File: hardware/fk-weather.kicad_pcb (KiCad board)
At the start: 2 copper layers, 26.2 x 121.2 mm, 65 parts, among them J1 RJ11-6, J2 MICRO-USB, J3 RJ11-6, J4 CONN-HDR-1x19, J5 CONN-HDR-1x19, J6 CONN-HDR-2x5, M1 MOUNT_HOLE, M2 MOUNT_HOLE, M3 MOUNT_HOLE, M4 MOUNT_HOLE, P1 CONN-HDR-MODULE, Q1 2N7002LT1G, SW1 SPNO, U1 ATSAMD21G18A-AU, U2 BQ24074RGTT, U4 MCP1700T-3302E/MB, Y1 FC-135

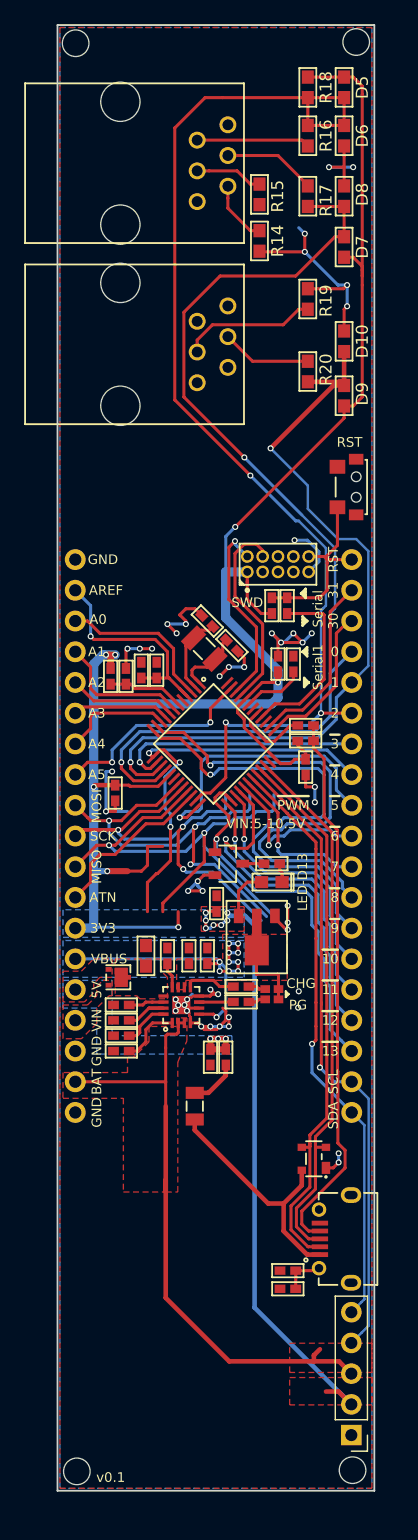
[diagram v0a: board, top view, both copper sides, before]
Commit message: Starting on the basic sensor module board. Just IC stuff.
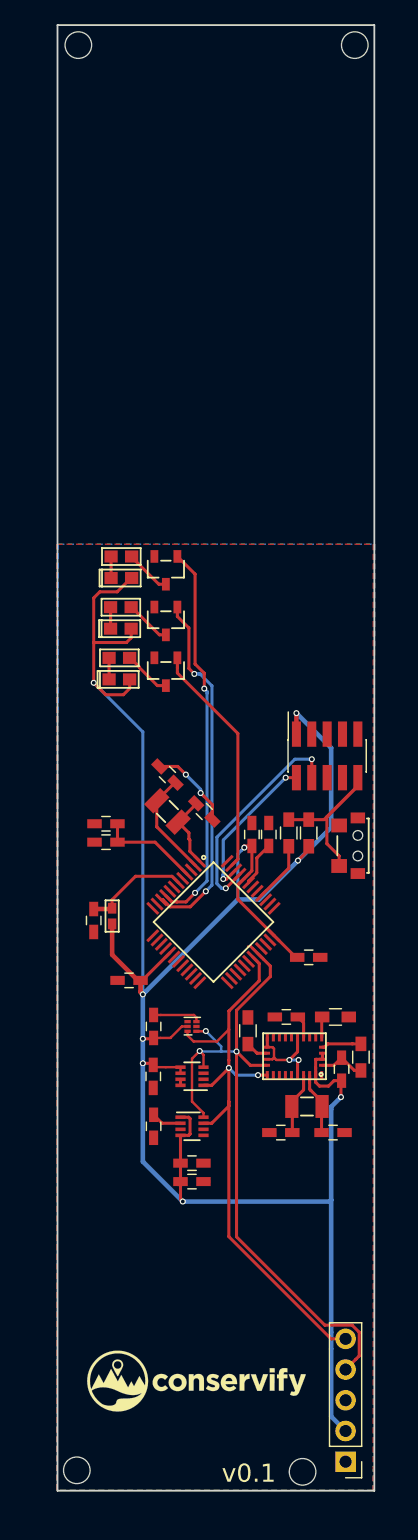
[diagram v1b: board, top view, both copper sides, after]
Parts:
- removed C10, C17: 4.7uF 10V X5R, RocketScreamKicadLibrary:CAP-0402
- removed C15, C19: 1uF 10V X5R, RocketScreamKicadLibrary:CAP-0402
- removed C18: 4.7nF 25V X7R, RocketScreamKicadLibrary:CAP-0402
- removed C9: 1uF 50V X5R, RocketScreamKicadLibrary:CAP-0603
- removed D10, D5, D6, D7, D8, D9: BAS16, RocketScreamKicadLibrary:DIO-0603
- removed D4: PMEG3020CPA, RocketScreamKicadLibrary:SOT-1016
- removed F1: MF-PSMF050X-2, RocketScreamKicadLibrary:MF-PSMF020X
- removed J1, J3: RJ11-6, fk-weather:molex_95501-2641
- removed J2: MICRO-USB, RocketScreamKicadLibrary:MICRO-USB
- removed J4, J5: CONN-HDR-1x19, RocketScreamKicadLibrary:HDR_1x19_Pitch2.54mm_WithoutSilk
- removed L1: BKP1005TS121-T, RocketScreamKicadLibrary:IND-0402
- removed P1: CONN-HDR-MODULE, fk-core-mini-ultra-pro:Socket_Strip_Straight_1x05_Pitch2.54mm
- removed R10, R13: 2K2, RocketScreamKicadLibrary:RES-0402
- removed R11: 100K, RocketScreamKicadLibrary:RES-0402
- removed R12, R8: 10K, RocketScreamKicadLibrary:RES-0402
- removed R14, R15, R16, R17, R19, R20: 1K, RocketScreamKicadLibrary:RES-0603
- removed R18: 4.7K, RocketScreamKicadLibrary:RES-0603
- removed R6: 1K18, RocketScreamKicadLibrary:RES-0402
- removed R7: 46K4, RocketScreamKicadLibrary:RES-0402
- removed R9: 2K94, RocketScreamKicadLibrary:RES-0402
- removed U2: BQ24074RGTT, RocketScreamKicadLibrary:QFN-16_3x3mm
- removed U4: MCP1700T-3302E/MB, RocketScreamKicadLibrary:SOT-89
- added C101: 1uF, Capacitors_SMD:C_0603_HandSoldering, F.Cu at (134.7, 114.8)
- added C102: 100nF, Capacitors_SMD:C_0603_HandSoldering, F.Cu at (134.7, 123.1)
- added C103: 100nF, Capacitors_SMD:C_0603_HandSoldering, F.Cu at (137.9, 127.6)
- added C104: 10uF, Capacitors_SMD:C_0603_HandSoldering, F.Cu at (137.9, 126.1)
- added C105: 22pF, Capacitors_SMD:C_0603_HandSoldering, F.Cu at (149.6, 123.6)
- added C106: 100nF, Capacitors_SMD:C_0603_HandSoldering, F.Cu at (150.3, 118.3)
- added C107: 22pF, Capacitors_SMD:C_0603_HandSoldering, F.Cu at (145.3, 123.6)
- added C108: 100nF, Capacitors_SMD:C_0603_HandSoldering, F.Cu at (145.7, 114.0)
- added C109: 100nF, Capacitors_SMD:C_0603_HandSoldering, F.Cu at (134.7, 118.9)
- added G***: LOGO, conservify:conservify_text_negative_4000, F.Cu at (138.3, 144.1)
- added P101: CONN_01X05, Socket_Strips:Socket_Strip_Straight_1x05_Pitch2.54mm, F.Cu at (150.6, 150.8)
- added Q2: 2N7002LT1G, RocketScreamKicadLibrary:SOT-23, F.Cu at (135.8, 81.3)
- added Q3: 2N7002LT1G, RocketScreamKicadLibrary:SOT-23, F.Cu at (135.8, 85.5)
- added R101: 10K, Resistors_SMD:R_0603_HandSoldering, F.Cu at (142.5, 115.2)
- added R102: 10K, Resistors_SMD:R_0603_HandSoldering, F.Cu at (149.8, 114.0)
- added R103: 10K, Resistors_SMD:R_0603_HandSoldering, F.Cu at (151.9, 117.3)
- added U101: TSL2591, Housings_DFN_QFN:DFN-6-1.3x1.2mm_Pitch0.4mm, F.Cu at (137.9, 114.8)
- added U102: MPL3115A2, Housings_DFN_QFN:DFN-8_2x2mm_Pitch0.5mm, F.Cu at (137.9, 123.1)
- added U103: BNO055, conservify:BNO055, F.Cu at (146.4, 117.3)
- added U104: SHT31, Housings_DFN_QFN:DFN-8_2x2mm_Pitch0.5mm, F.Cu at (137.9, 118.9)
- added Y101: FC-135, RocketScreamKicadLibrary:ABS07, F.Cu at (147.4, 121.4)
- C1, C14, C2, C3, C4, C5, C6, C7, C8: footprint RocketScreamKicadLibrary:CAP-0402 -> Capacitors_SMD:C_0603_HandSoldering
- D2: value LED-DUAL -> Yellow; footprint RocketScreamKicadLibrary:LED-1615 -> RocketScreamKicadLibrary:LED-0603
- D3: value PRTR5V0U2X -> Blue; footprint RocketScreamKicadLibrary:SOT-143B -> RocketScreamKicadLibrary:LED-0603
- J6: footprint RocketScreamKicadLibrary:HDR_2x5_Pitch1.27mm -> Socket_Strips:Socket_Strip_Straight_2x05_Pitch1.27mm_SMD
- R1: value 2K2 -> 2k2; footprint RocketScreamKicadLibrary:RES-0402 -> RocketScreamKicadLibrary:RES-0603
- R2, R4: footprint RocketScreamKicadLibrary:RES-0402 -> Resistors_SMD:R_0603_HandSoldering
- R3: value 330R -> 2k2; footprint RocketScreamKicadLibrary:RES-0402 -> RocketScreamKicadLibrary:RES-0603
- R5: value 1M -> 2k2; footprint RocketScreamKicadLibrary:RES-0402 -> RocketScreamKicadLibrary:RES-0603
- moved M4 120.3 mm to (128.4, 151.5)
- moved M2 117.8 mm to (151.4, 33.7)
- moved R5 54.0 mm to (131.9, 84.3), turned to 0 degrees
- moved D3 42.8 mm to (131.9, 86.1), turned to 0 degrees
- moved D2 32.7 mm to (132.0, 81.9), turned to 0 degrees
- moved SW1 29.7 mm to (151.8, 99.9)
- moved R1 28.3 mm to (132.1, 75.9), turned to 0 degrees
- moved D1 28.1 mm to (132.1, 77.7), turned to 0 degrees
- moved Q1 24.8 mm to (135.8, 77.1), turned to 180 degrees
- moved C4 20.4 mm to (129.8, 106.0), turned to 270 degrees
- moved L2 19.8 mm to (131.3, 105.7), turned to 270 degrees
- moved R4 19.0 mm to (147.6, 98.8)
- moved R2 18.8 mm to (145.9, 98.8)
- moved M1 18.7 mm to (147.1, 151.6)
- moved R3 18.1 mm to (132.0, 80.1), turned to 0 degrees
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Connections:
- D2 pad 1: VBUS -> Net-(D2-Pad1)
- D2 pad 2: VBUS -> 3V3
- D3 pad 1: GND -> Net-(D3-Pad1)
- D3 pad 2: /USB+ -> 3V3
- J6 pad 6: (no net) -> Net-(J6-Pad6)
- J6 pad 7: (no net) -> Net-(J6-Pad7)
- J6 pad 8: (no net) -> Net-(J6-Pad8)
- Q1 pad 1: /D13 -> /A3
- R3 pad 1: Net-(J2-Pad4) -> Net-(D2-Pad1)
- R3 pad 2: /USB_ID -> Net-(Q2-Pad3)
- R5 pad 1: Net-(C18-Pad1) -> Net-(D3-Pad1)
- R5 pad 2: GND -> Net-(Q3-Pad3)
- U1 pad 26: /D13 -> Net-(U1-Pad26)
- U1 pad 39: (no net) -> /TX_LED
- U1 pad 48: (no net) -> /RX_LED
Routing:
- net /D2: track 95.3 -> 0.00 mm, vias 3 -> 0
- net /D0: track 87.0 -> 0.00 mm, vias 2 -> 0
- net /D1: track 64.8 -> 0.00 mm, vias 2 -> 0
- net GND: track 86.0 -> 24.6 mm, vias 46 -> 4
- net VBAT: track 51.7 -> 0.00 mm
- net Net-(J2-Pad4): track 45.5 -> 0.00 mm
- net /USB-: track 45.4 -> 0.00 mm
- net /MISO: track 45.3 -> 0.00 mm, vias 2 -> 0
- net /USB+: track 44.8 -> 0.00 mm
- net /D9: track 40.2 -> 0.00 mm, vias 1 -> 0
- net /SCK: track 37.4 -> 0.00 mm, vias 3 -> 0
- net /MOSI: track 37.2 -> 0.00 mm, vias 3 -> 0
- net /D8: track 37.0 -> 0.00 mm, vias 1 -> 0
- net VBUS: track 35.4 -> 0.00 mm, vias 11 -> 0
- net /D4: track 35.0 -> 0.00 mm, vias 3 -> 0
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- removed copper zone on B.Cu, net 3V3
- removed copper zone on F.Cu, net 3V3
- removed copper zone on B.Cu, net 5V0
- removed copper zone on F.Cu, net 5V0
- removed copper zone on F.Cu, net VBAT
- removed copper zone on B.Cu, net VBUS
- removed copper zone on F.Cu, net VBUS
- removed copper zone on F.Cu, net VEXT
- removed copper zone on F.Cu, net VIN
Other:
- board text removed: "0"
- board text removed: "1"
- board text removed: "10"
- board text removed: "11"
- board text removed: "12"
- board text removed: "13"
- board text removed: "2"
- board text removed: "3"
- board text removed: "30"
- board text removed: "31"
- board text removed: "3V3"
- board text removed: "4"
- board text removed: "5"
- board text removed: "5V"
- board text removed: "6"
- board text removed: "7"
- board text removed: "8"
- board text removed: "9"
- board text removed: "A0"
- board text removed: "A1"
- board text removed: "A2"
- board text removed: "A3"
- board text removed: "A4"
- board text removed: "A5"
- board text removed: "AREF"
- board text removed: "ATN"
- board text removed: "BAT"
- board text removed: "CHG"
- board text removed: "GND"
- board text removed: "LED-D13"
- board text removed: "MISO"
- board text removed: "MOSI"
- board text removed: "PG"
- board text removed: "PWM"
- board text removed: "RST"
- board text removed: "SCK"
- board text removed: "SCL"
- board text removed: "SDA"
- board text removed: "SWD"
- board text removed: "Serial"
- board text removed: "Serial1"
- board text removed: "VBUS"
- board text removed: "VIN"
- board text removed: "VIN:5-10.5V"

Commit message: Adding pull ups, fixing the outline. Plotting.
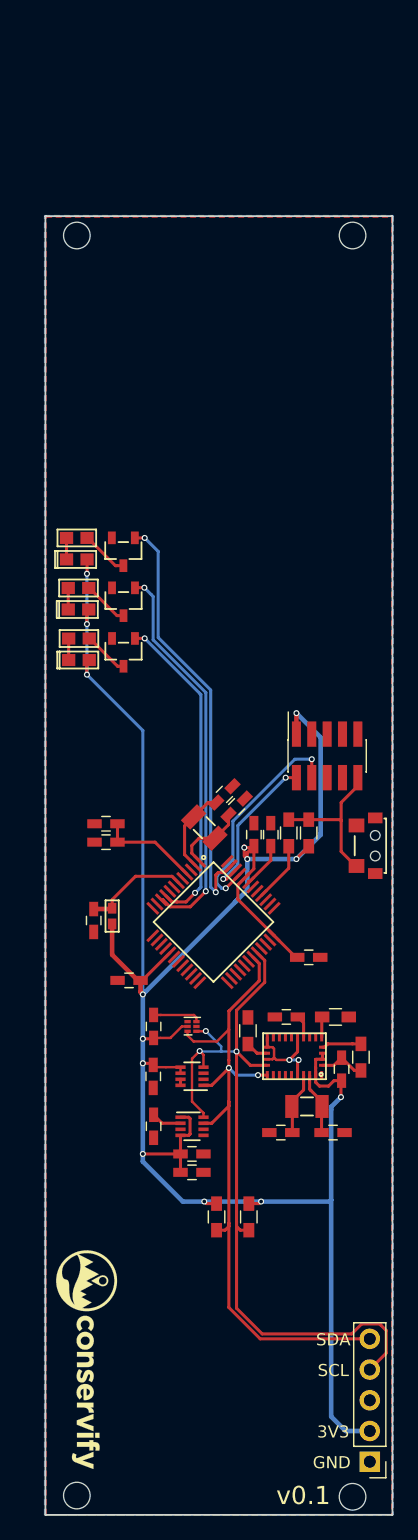
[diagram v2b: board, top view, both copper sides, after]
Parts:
- added R6: 4.7k, Resistors_SMD:R_0603_HandSoldering, F.Cu at (140.0, 130.6)
- added R7: 4.7k, Resistors_SMD:R_0603_HandSoldering, F.Cu at (142.6, 130.6)
- moved M2 120.0 mm to (151.2, 153.7)
- moved M4 104.6 mm to (151.2, 49.4)
- moved M1 18.8 mm to (128.4, 153.6)
- moved M3 15.7 mm to (128.4, 49.4)
- moved D3 10.5 mm to (128.4, 76.2)
- moved Q3 10.5 mm to (132.2, 75.6)
- moved R5 10.5 mm to (128.4, 74.4)
- moved G*** 9.28 mm to (129.2, 142.4), turned to 270 degrees
- moved Q1 7.63 mm to (132.3, 83.9)
- moved R1 7.63 mm to (128.6, 82.7)
- moved D1 7.63 mm to (128.6, 84.5)
- moved C1 4.99 mm to (140.6, 95.6), turned to 225 degrees
- moved D2 3.85 mm to (128.5, 80.3)
- moved R3 3.85 mm to (128.5, 78.5)
- moved Q2 3.85 mm to (132.3, 79.7)
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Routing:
- net /A5: track 19.5 -> 35.6 mm, vias 0 -> 2
- net GND: track 24.6 -> 17.1 mm, vias 4 -> 2
- net /SDA: track 51.1 -> 57.9 mm
- net /SCL: track 59.6 -> 66.4 mm
- net /A3: track 32.2 -> 26.9 mm
- net /A4: track 29.6 -> 32.4 mm
- net /RST: track 15.7 -> 13.0 mm
- net 3V3: track 193.0 -> 190.6 mm, vias 9 -> 14
- net Net-(C1-Pad2): track 8.86 -> 7.08 mm
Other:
- board size 26.2 x 121.2 mm -> 28.7 x 107.4 mm
- board text added: "3V3"
- board text added: "GND"
- board text added: "SCL"
- board text added: "SDA"

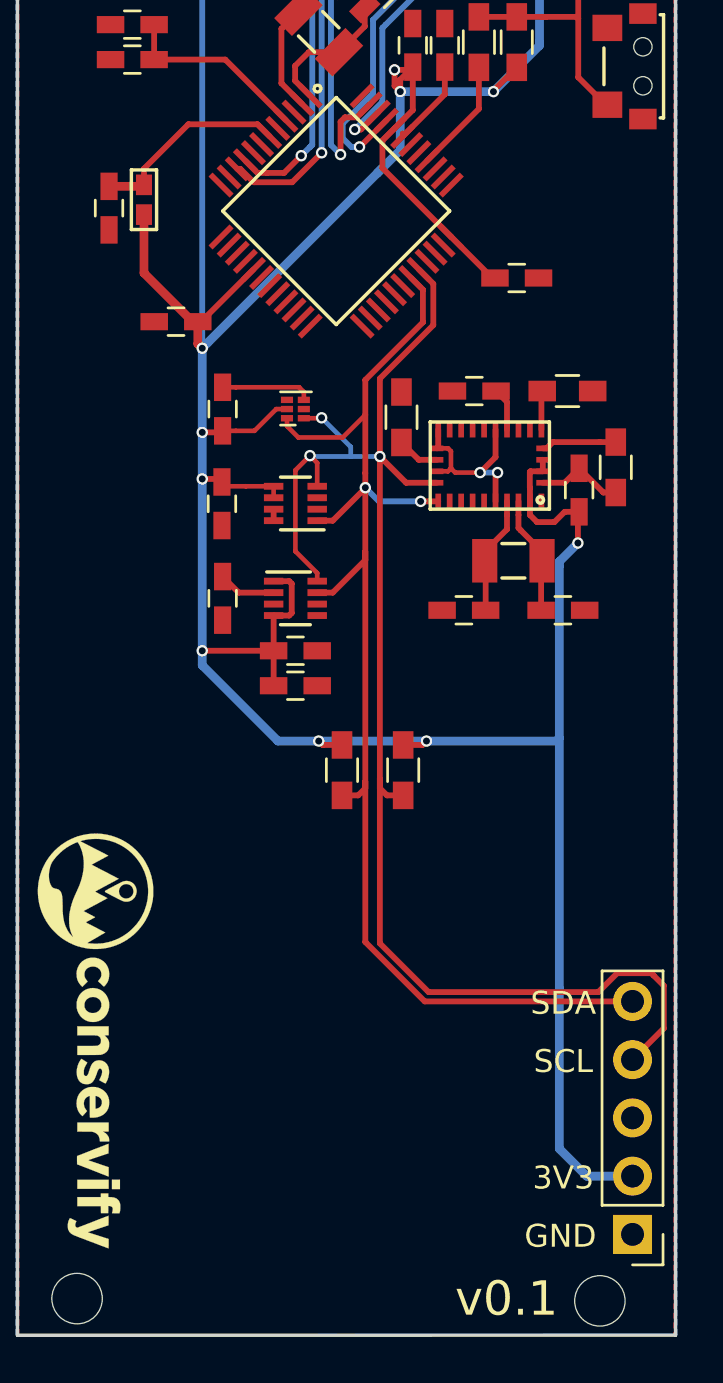
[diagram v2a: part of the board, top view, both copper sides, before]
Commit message: Adding USB connector and 3v3 regulator.
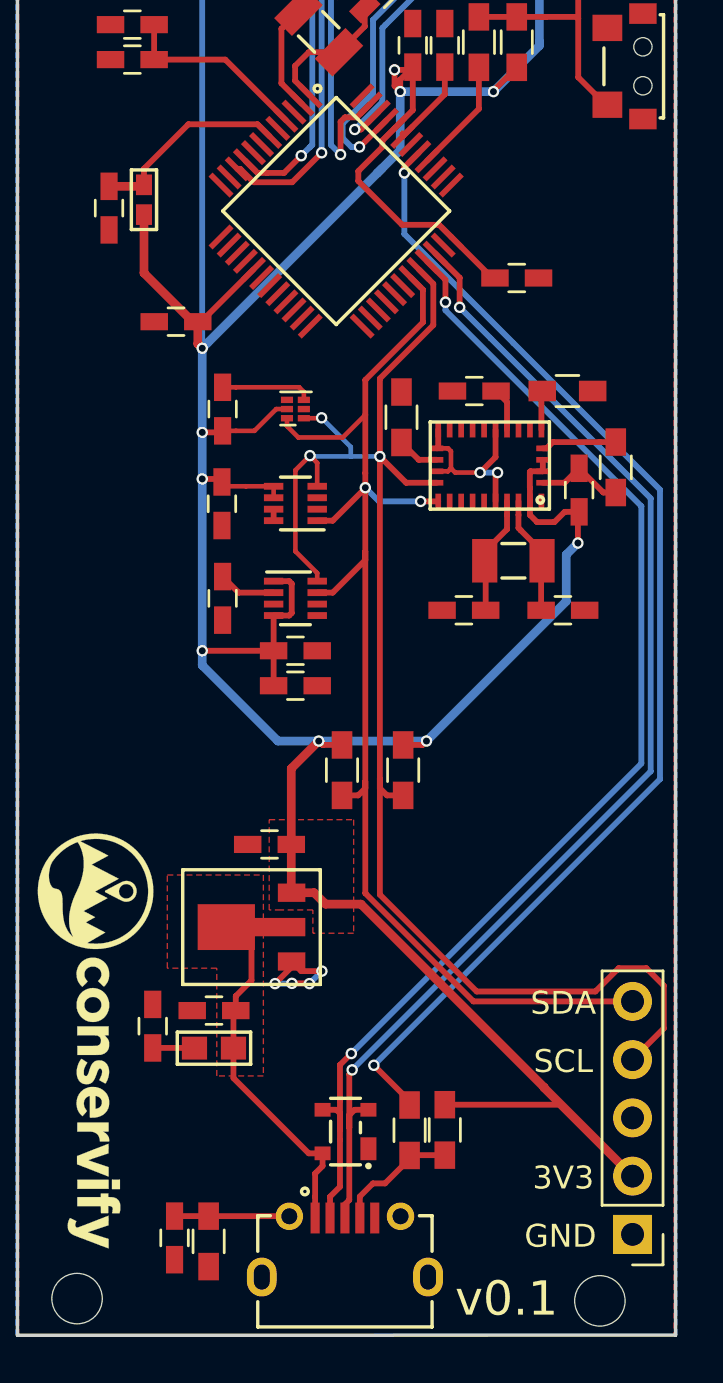
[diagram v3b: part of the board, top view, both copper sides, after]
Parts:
- added C10: 4.7nF, Capacitors_SMD:C_0603_HandSoldering, F.Cu at (132.7, 151.0)
- added C11: 1uF, Capacitors_SMD:C_0603_HandSoldering, F.Cu at (134.4, 141.0)
- added C12: 1uF, Capacitors_SMD:C_0603_HandSoldering, F.Cu at (136.8, 133.8)
- added C9: 4.7uF, Capacitors_SMD:C_0603_HandSoldering, F.Cu at (131.7, 141.7)
- added D4: PRTR5V0U2X, RocketScreamKicadLibrary:SOT-143B, F.Cu at (140.1, 146.3)
- added J1: MICRO-USB, RocketScreamKicadLibrary:MICRO-USB, F.Cu at (140.1, 151.5)
- added L1: MF-PSMF050x-2, RocketScreamKicadLibrary:IND-0603, F.Cu at (134.4, 142.7)
- added R10: 1M, Resistors_SMD:R_0603_HandSoldering, F.Cu at (134.1, 151.1)
- added R8: 100k, Resistors_SMD:R_0603_HandSoldering, F.Cu at (144.4, 146.2)
- added R9: 330R, Resistors_SMD:R_0603_HandSoldering, F.Cu at (142.9, 146.3)
- added U2: MCP1700T-XXX2E, RocketScreamKicadLibrary:SOT-89, F.Cu at (136.0, 137.4)
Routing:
- net /USB+: track 0.00 -> 53.0 mm, vias 0 -> 2
- net /USB-: track 0.00 -> 52.8 mm, vias 0 -> 2
- net /USB_ID: track 0.00 -> 52.2 mm, vias 0 -> 2
- net VUSB: track 0.00 -> 16.2 mm
- net 3V3: track 190.6 -> 203.6 mm
- net Net-(J1-Pad4): track 0.00 -> 5.48 mm
- net GND: track 17.1 -> 22.1 mm, vias 2 -> 6
- net Net-(C10-Pad1): track 0.00 -> 5.04 mm
- net 5V0: track 0.00 -> 1.81 mm
- net /SDA: track 57.9 -> 56.7 mm
- net /SCL: track 66.4 -> 65.3 mm
- added copper zone on F.Cu, net 3V3
- added copper zone on F.Cu, net VUSB

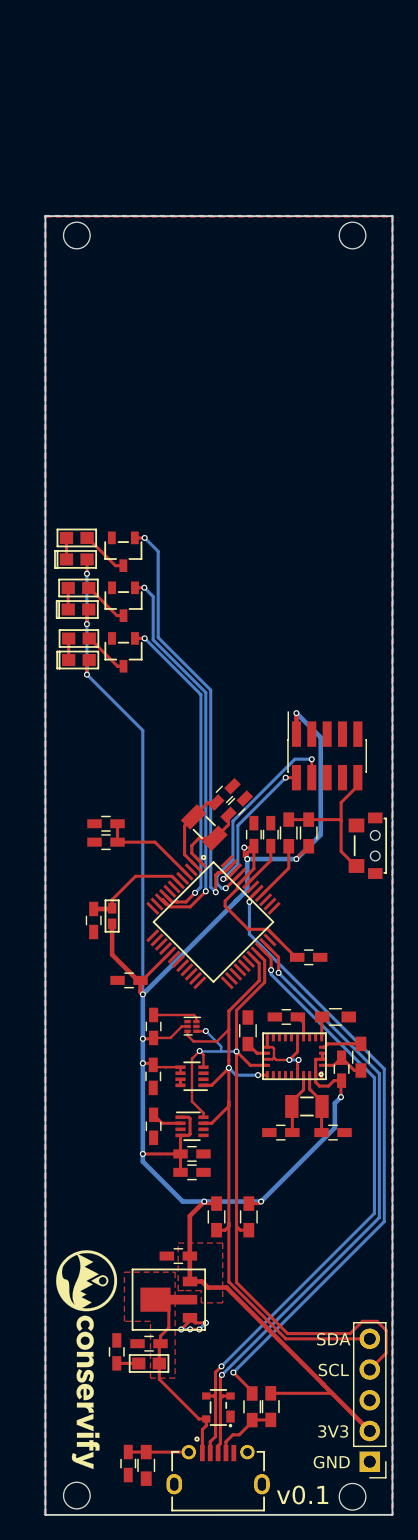
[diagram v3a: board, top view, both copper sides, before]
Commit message: Adding MAX4466.
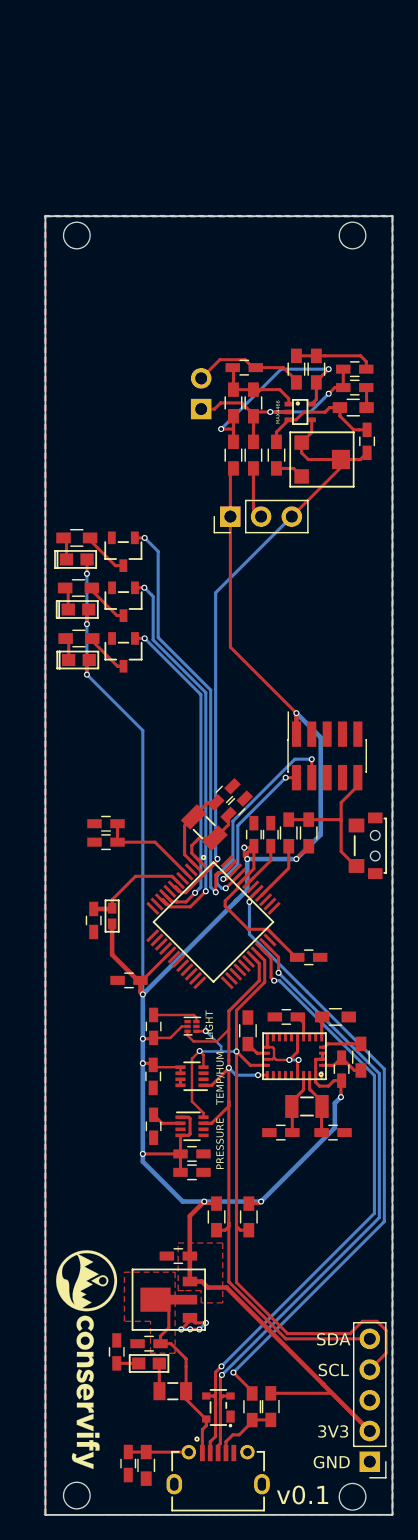
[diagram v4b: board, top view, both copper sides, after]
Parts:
- added C13: 0.1uF, Capacitors_SMD:C_0603_HandSoldering, F.Cu at (151.4, 60.5)
- added C15: 0.01uF, Capacitors_SMD:C_0603_HandSoldering, F.Cu at (142.2, 60.3)
- added C16: 10uF, Capacitors_SMD:C_0603_HandSoldering, F.Cu at (151.4, 62.0)
- added C17: 100pF, Capacitors_SMD:C_0603_HandSoldering, F.Cu at (152.4, 66.4)
- added F1: MF-PSMF050X-2, RocketScreamKicadLibrary:MF-PSMF020X, F.Cu at (136.3, 145.0)
- added J2: CONN_01X03, Socket_Strips:Socket_Strip_Straight_1x03_Pitch2.54mm, F.Cu at (141.1, 72.6)
- added L3: ?, Resistors_SMD:R_0603_HandSoldering, F.Cu at (141.4, 67.6)
- added L4: ?, Resistors_SMD:R_0603_HandSoldering, F.Cu at (143.0, 67.6)
- added MK1: CMA-4544PF-W, Socket_Strips:Socket_Strip_Angled_1x02_Pitch2.54mm, B.Cu at (138.7, 63.8)
- added R11: 1k, Resistors_SMD:R_0603_HandSoldering, F.Cu at (148.2, 60.5)
- added R12: 1k, Resistors_SMD:R_0603_HandSoldering, F.Cu at (146.6, 60.5)
- added R13: 1k, Resistors_SMD:R_0603_HandSoldering, F.Cu at (151.3, 63.6)
- added R14: 1M, Resistors_SMD:R_0603_HandSoldering, F.Cu at (141.4, 63.2)
- added R15: 1M, Resistors_SMD:R_0603_HandSoldering, F.Cu at (143.0, 63.2)
- added R16: 22k, Resistors_SMD:R_0603_HandSoldering, F.Cu at (144.9, 67.6)
- added RV1: TC33X-2-104E (100K), conservify:BOURNS-TC33X-2, F.Cu at (148.8, 67.9)
- added U3: MAX4466, conservify:SC70-5, F.Cu at (146.9, 64.0)
- L1: value MF-PSMF050x-2 -> BKP1005TS121-T
- R1, R3, R5: footprint RocketScreamKicadLibrary:RES-0603 -> Resistors_SMD:R_0603_HandSoldering
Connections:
- L1 pad 2: VUSB -> Net-(F1-Pad1)
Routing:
- net /A1: track 0.00 -> 51.4 mm, vias 0 -> 1
- net 3V3: track 203.6 -> 226.2 mm
- net /AGND: track 0.00 -> 18.7 mm, vias 0 -> 2
- net /AVCC: track 0.00 -> 17.5 mm, vias 0 -> 2
- net Net-(C17-Pad2): track 0.00 -> 10.3 mm
- net Net-(C15-Pad2): track 0.00 -> 9.38 mm
- net Net-(C15-Pad1): track 0.00 -> 7.18 mm
- net Net-(C13-Pad1): track 0.00 -> 6.60 mm
- net GND: track 22.1 -> 26.3 mm
- net Net-(R16-Pad1): track 0.00 -> 2.36 mm
- net Net-(F1-Pad1): track 0.00 -> 2.31 mm
- net Net-(C16-Pad2): track 0.00 -> 1.66 mm
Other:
- board text added: "LIGHT"
- board text added: "PRESSURE"
- board text added: "TEMP/HUM"
